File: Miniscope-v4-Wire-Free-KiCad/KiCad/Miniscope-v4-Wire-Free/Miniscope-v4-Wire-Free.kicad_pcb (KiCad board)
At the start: 6 copper layers, 27.6 x 12.2 mm, 114 parts, among them J1 0475710001, J10 Conn_01x01, J11 Conn_01x01, J12 Conn_01x01, J14 Conn_01x01, J15 Conn_01x01, J16 Conn_01x01, J17 Conn_01x01, J18 Conn_01x01, J19 Conn_01x01, J2 Conn_01x04, J20 Conn_01x01, J21 Conn_01x01, J22 Conn_01x01, J23 Conn_01x01, J24 Conn_01x01, J25 Conn_01x01, J26 Conn_01x01, J27 Conn_01x01, J3 Conn_01x04, J4 Conn_01x01, J5 Conn_01x01, J6 Conn_01x01, J7 Conn_01x01, J8 Conn_01x01, J9 Conn_01x01, Q1 NTK3134NT1G, Q2 MMBT3904LP-7B, SW1 TL3780AF330QG, U1 LTC3554, U2 HV892, U3 LTC3218, U4 MAX13030EETE+BGA, U5 TSOP57438TT1, U6 ATSAMD51J20A-UUT-EFP, U7 NCP163AMX330TBG, U8 NOIP1SN0480A, U9 LMV321IDCKR, Y2 Crystal

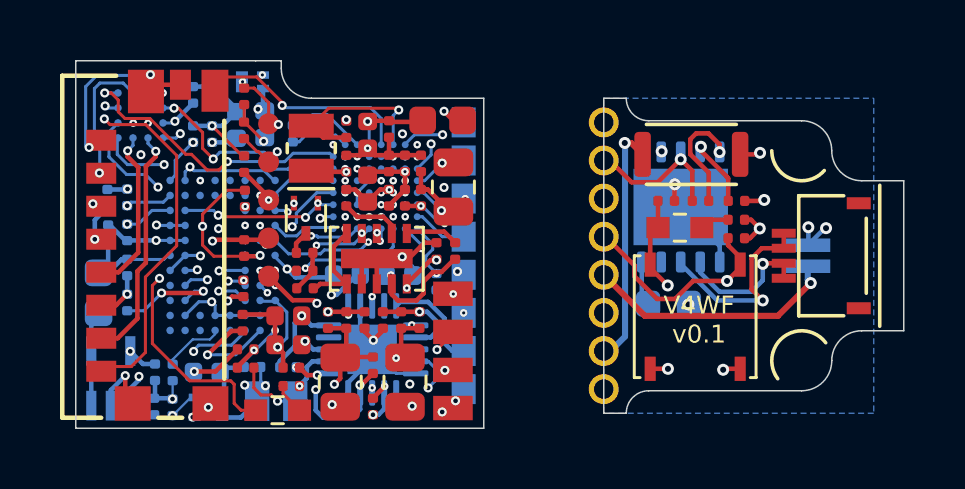
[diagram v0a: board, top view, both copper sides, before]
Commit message: Updates to the jupyter notebooks
- Added capability to recover the timestamps from the recording and generate a comma separated value file
- Added the pullup resistor to the reset line of the MCU in the PCB.
- Added the gerbers used for the batch fabrication
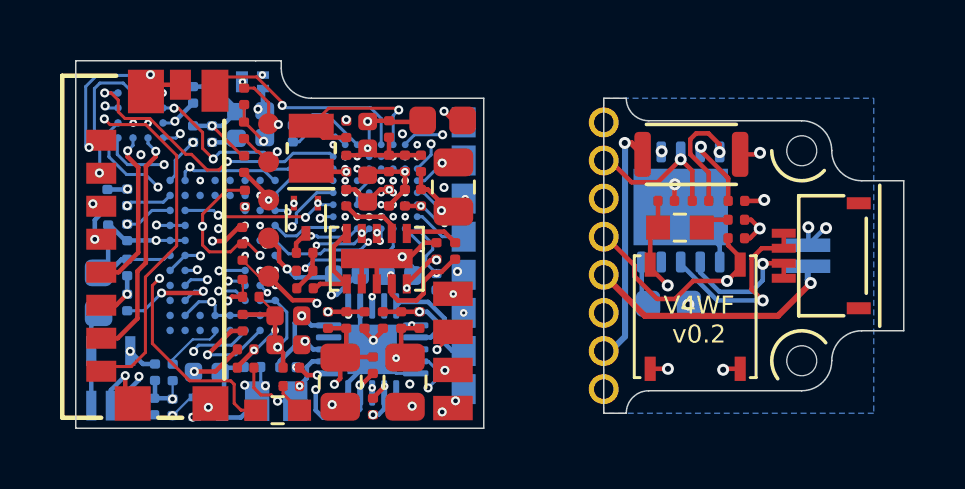
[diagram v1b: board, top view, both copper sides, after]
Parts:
- added ?: , , F.Cu at (103.6, 61.0)
- added R22: 10K, Resistor_SMD:R_0201_0603Metric, F.Cu at (85.0, 65.0)
- added REF**: MountingHole_2.1mm, MountingHole:MountingHole_2.1mm, F.Cu at (103.6, 67.9)
- D1: value LXZ1-PR01 -> LXZ1-PB01
- moved C42 0.42 mm to (85.0, 63.8)
- moved C43 0.37 mm to (85.2, 65.9), turned to 0 degrees
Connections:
- U1 pad 19: Net-(U1-Pad19) -> unconnected-(U1-SUSP-Pad19)
- U1 pad 4: Net-(U1-Pad4) -> unconnected-(U1-PGOOD-Pad4)
- U2 pad 9: Net-(U2-Pad9) -> unconnected-(U2-NC-Pad9)
- U6 pad B3: Net-(U6-PadB3) -> unconnected-(U6A-PA27-PadB3)
- U6 pad B6: Net-(U6-PadB6) -> unconnected-(U6A-PB31-PadB6)
- U6 pad C6: Net-(U6-PadC6) -> unconnected-(U6A-PB03-PadC6)
- U6 pad D6: Net-(U6-PadD6) -> unconnected-(U6A-PA03-PadD6)
- U6 pad D7: Net-(U6-PadD7) -> unconnected-(U6A-PB04-PadD7)
- U6 pad E6: Net-(U6-PadE6) -> unconnected-(U6A-PB07-PadE6)
- U6 pad E7: Net-(U6-PadE7) -> unconnected-(U6A-PB06-PadE7)
- U6 pad F5: Net-(U6-PadF5) -> unconnected-(U6A-PB08-PadF5)
- U8 pad B11: Net-(U8-PadB11) -> unconnected-(U8-CLK_OUTP-PadB11)
- U8 pad B9: Net-(U8-PadB9) -> unconnected-(U8-DOUT0-PadB9)
- U8 pad C10: Net-(U8-PadC10) -> unconnected-(U8-CLK_OUTN-PadC10)
- U8 pad C11: Net-(U8-PadC11) -> unconnected-(U8-DOUTP-PadC11)
- U8 pad C9: Net-(U8-PadC9) -> unconnected-(U8-DOUT1-PadC9)
- U8 pad D10: Net-(U8-PadD10) -> unconnected-(U8-DOUTN-PadD10)
- U8 pad D11: Net-(U8-PadD11) -> unconnected-(U8-SYNCP-PadD11)
- U8 pad E10: Net-(U8-PadE10) -> unconnected-(U8-SYNCN-PadE10)
- U8 pad E11: Net-(U8-PadE11) -> unconnected-(U8-LVDS_CLK_INP-PadE11)
- U8 pad F1: Net-(U8-PadF1) -> unconnected-(U8-CP_RESPD-PadF1)
- U8 pad F10: Net-(U8-PadF10) -> unconnected-(U8-LVDS_CLK_INN-PadF10)
- U8 pad G1: Net-(U8-PadG1) -> unconnected-(U8-CP_CALIB-PadG1)
- U8 pad H1: Net-(U8-PadH1) -> unconnected-(U8-MBSINOUT1-PadH1)
- U8 pad H2: Net-(U8-PadH2) -> unconnected-(U8-MBSINOUT1-PadH2)
- U8 pad H3: Net-(U8-PadH3) -> unconnected-(U8-MBSINOUT2-PadH3)
- U8 pad H4: Net-(U8-PadH4) -> unconnected-(U8-CP_SEL_SAMPLE-PadH4)
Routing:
- net GND: track 80.9 -> 82.4 mm, vias 46 -> 45
- net /nRESET: track 8.70 -> 9.79 mm
- net +1V8: track 62.4 -> 63.0 mm
- net /SPI1_NSS: vias 4 -> 3
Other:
- rule pad_to_mask_clearance: 0.0254 -> 0
- board text added: "V4WF v0.2"
- board text removed: "V4WF v0.1"

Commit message: Added new gerbers for the fabrication outputs for version 1.0
- Generated new fabrication outputs for the v1.0
- Corrected the resistor value for the reset pull up resistor (from 1k to 10k)
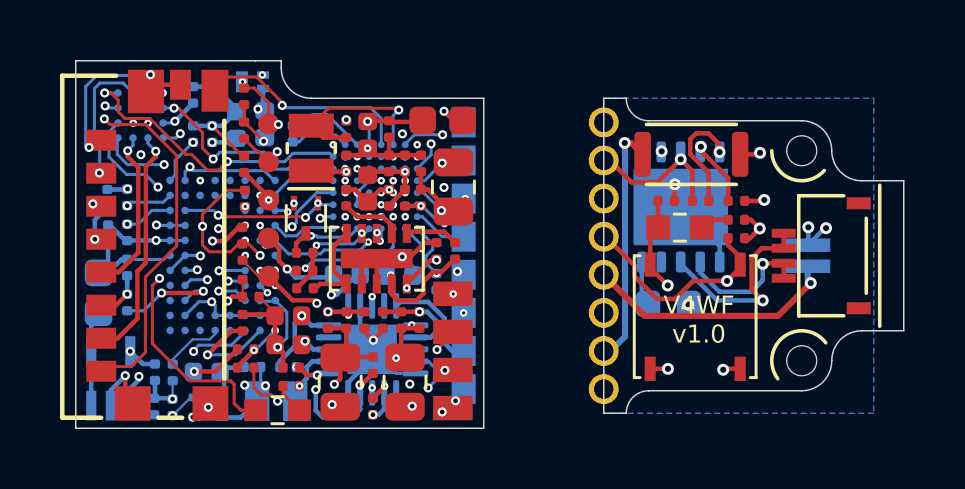
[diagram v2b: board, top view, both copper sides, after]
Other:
- board text added: "V4WF v1.0"
- board text removed: "V4WF v0.2"
